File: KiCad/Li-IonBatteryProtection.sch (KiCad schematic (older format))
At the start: 55 parts, among them J1 CONN_02X03, J2 CONN_01X02, Q1 IRF540N, Q2 2N2222A, Q3 2N2222A, Q4 2N2222A, Q5 2N2222A, Q6 2N2222A, U1 LM311N, U2 PC817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

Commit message: Updated the TO-220 footprint. Started fill zones.
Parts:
- Q1: footprint TO_SOT_Packages_THT:TO-220_Neutral123_Horizontal_LargePads -> TO_SOT_Packages_THT:TO-220_Neutral123_Horizontal
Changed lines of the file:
@@
 F 0 "Q1" H 7950 3850 50  0000 L CNN
 F 1 "IRF540N" H 7450 3400 50  0000 L CNN
-F 2 "TO_SOT_Packages_THT:TO-220_Neutral123_Horizontal_LargePads" H 8000 3575 50  0001 L CIN
+F 2 "TO_SOT_Packages_THT:TO-220_Neutral123_Horizontal" H 8000 3575 50  0001 L CIN
 F 3 "" H 7750 3650 50  0000 L CNN
 	1    7750 3650

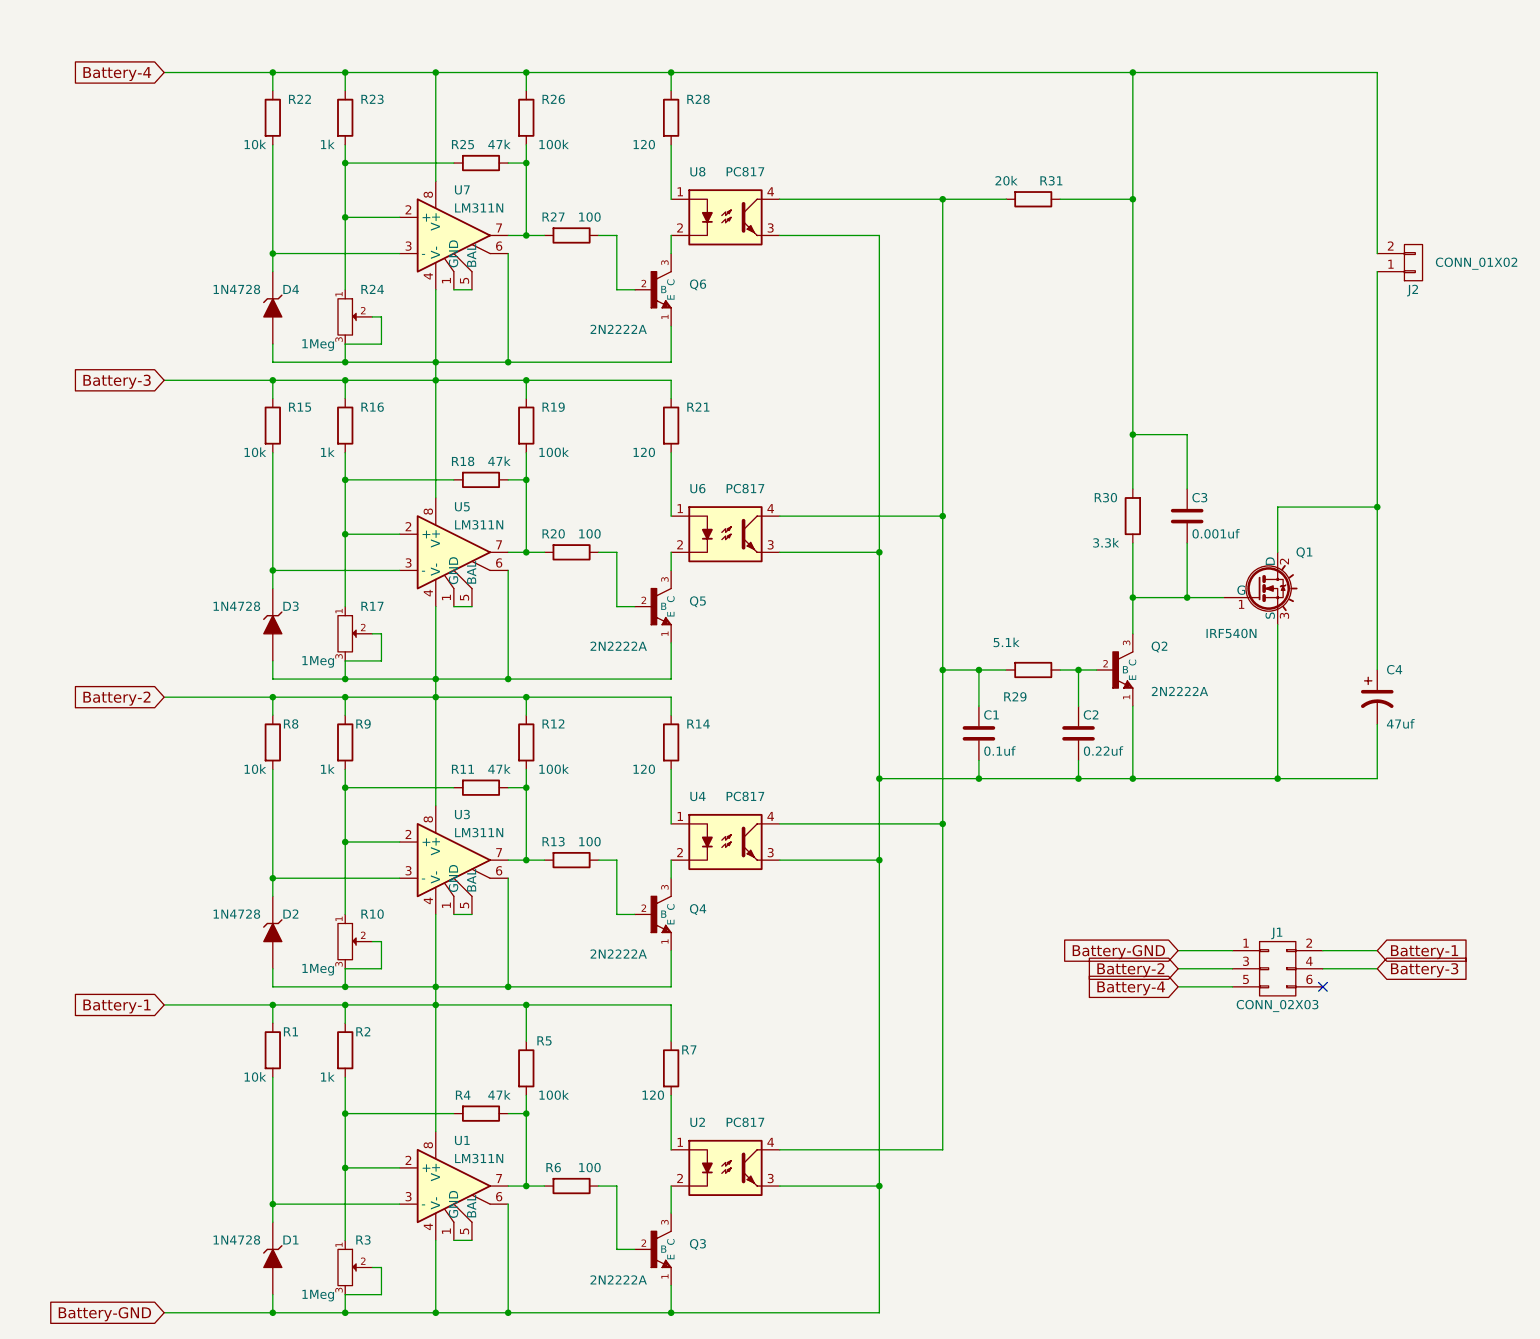
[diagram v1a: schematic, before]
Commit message: Added test points to the schematic.
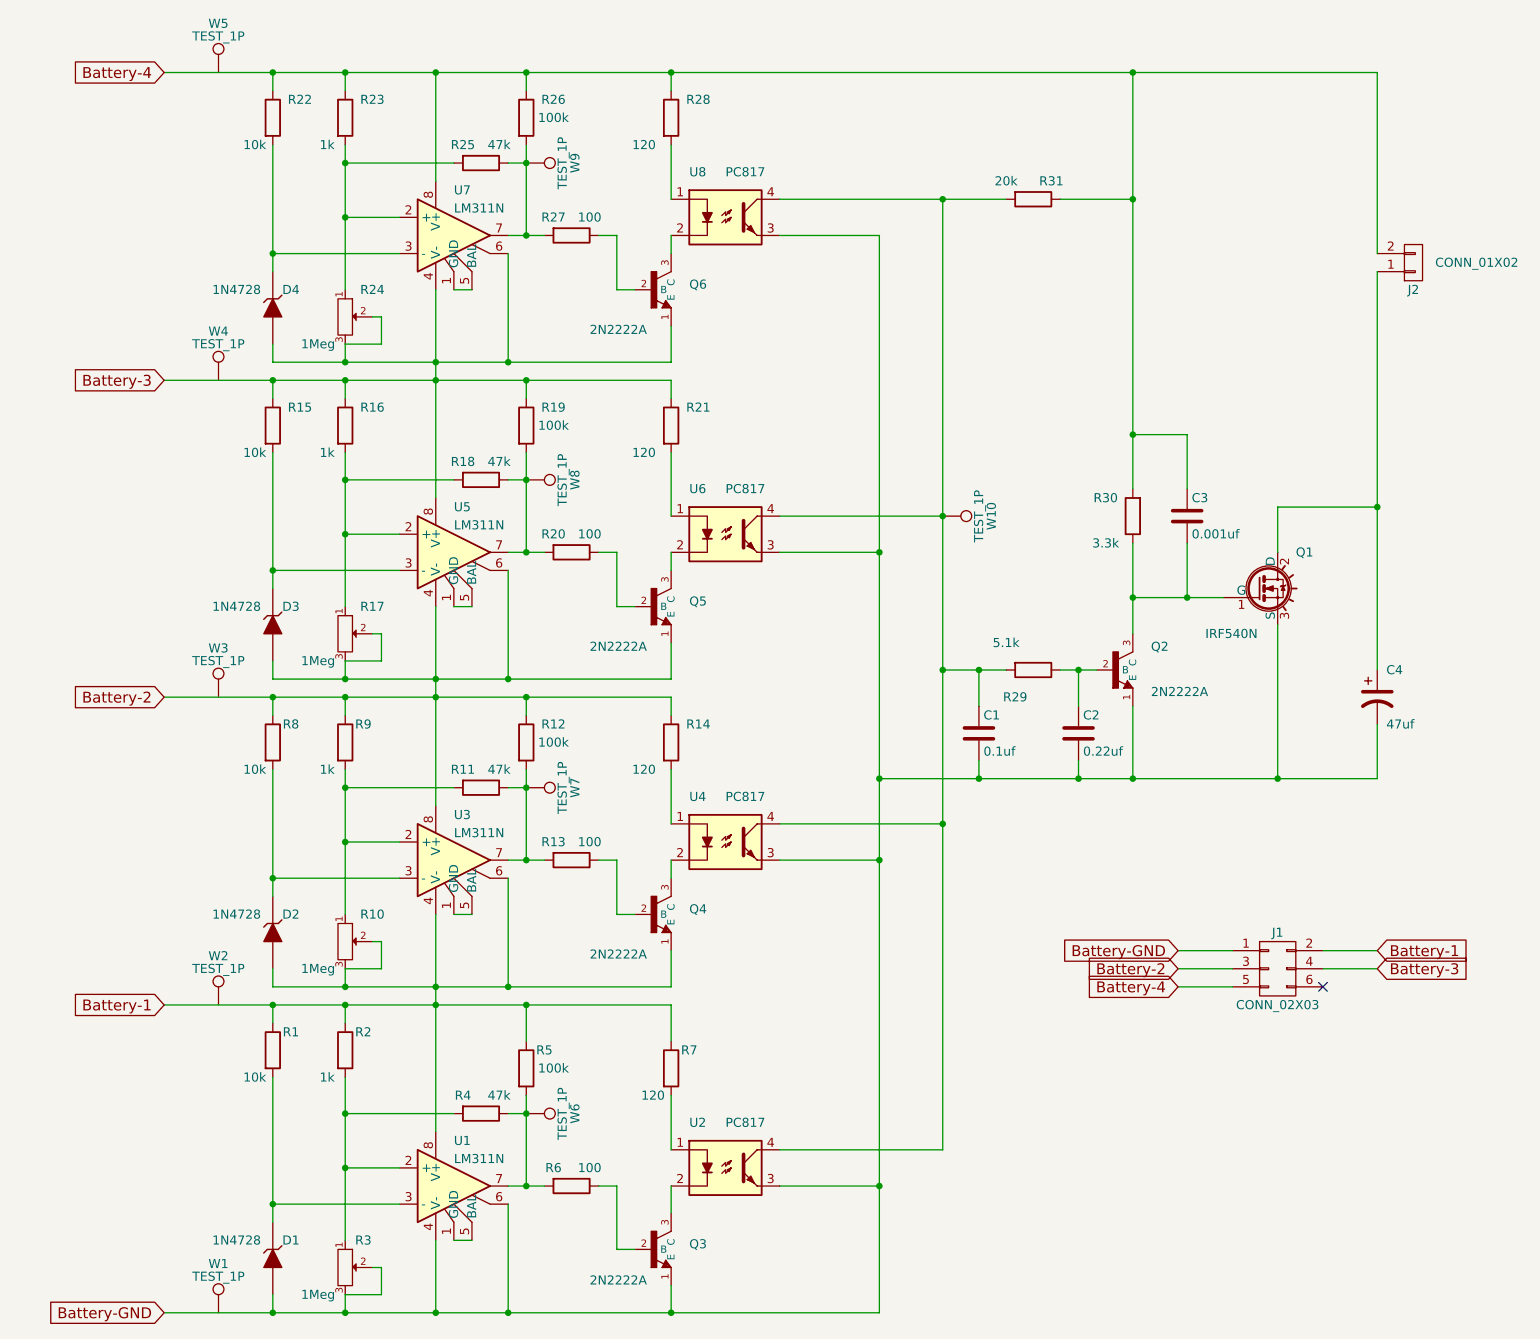
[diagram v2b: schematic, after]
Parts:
- added W1, W10, W2, W3, W4, W5, W6, W7, W8, W9: TEST_1P, Measurement_Points:Measurement_Point_Round-TH_Big, symbol TEST_1P
- R16, R2, R23, R9: footprint Resistors_ThroughHole:Resistor_Horizontal_RM7mm -> Resistors_ThroughHole:Resistor_Horizontal_RM10mm
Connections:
- net at C1.1, R29.2, R31.2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: now also W10.1
- net at R4.1, R5.2, R6.2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: now also W6.1
- net at R11.1, R12.2, R13.2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: now also W7.1
- net at R18.1, R19.2, R20.2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: now also W8.1
- net at R25.1, R26.2, R27.2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: now also W9.1
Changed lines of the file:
@@
 F 0 "R2" H 2800 6300 50  0000 C CNN
 F 1 "1k" H 2600 6050 50  0000 C CNN
-F 2 "Resistors_ThroughHole:Resistor_Horizontal_RM7mm" V 2630 6200 50  0001 C CNN
+F 2 "Resistors_ThroughHole:Resistor_Horizontal_RM10mm" V 2630 6200 50  0001 C CNN
 F 3 "" H 2700 6200 50  0000 C CNN
 	1    2700 6200
@@
 U 1 1 592CD4C8
 P 3700 6300
-F 0 "R5" H 3800 6450 50  0000 C CNN
-F 1 "100k" H 3850 6150 50  0000 C CNN
+F 0 "R5" H 3800 6400 50  0000 C CNN
+F 1 "100k" H 3850 6300 50  0000 C CNN
 F 2 "Resistors_ThroughHole:Resistor_Horizontal_RM10mm" V 3630 6300 50  0001 C CNN
 F 3 "" H 3700 6300 50  0000 C CNN
@@
 F 0 "R9" H 2800 4600 50  0000 C CNN
 F 1 "1k" H 2600 4350 50  0000 C CNN
-F 2 "Resistors_ThroughHole:Resistor_Horizontal_RM7mm" V 2630 4500 50  0001 C CNN
+F 2 "Resistors_ThroughHole:Resistor_Horizontal_RM10mm" V 2630 4500 50  0001 C CNN
 F 3 "" H 2700 4500 50  0000 C CNN
 	1    2700 4500
@@
 P 3700 4500
 F 0 "R12" H 3850 4600 50  0000 C CNN
-F 1 "100k" H 3850 4350 50  0000 C CNN
+F 1 "100k" H 3850 4500 50  0000 C CNN
 F 2 "Resistors_ThroughHole:Resistor_Horizontal_RM10mm" V 3630 4500 50  0001 C CNN
 F 3 "" H 3700 4500 50  0000 C CNN
@@
 F 0 "R16" H 2850 2850 50  0000 C CNN
 F 1 "1k" H 2600 2600 50  0000 C CNN
-F 2 "Resistors_ThroughHole:Resistor_Horizontal_RM7mm" V 2630 2750 50  0001 C CNN
+F 2 "Resistors_ThroughHole:Resistor_Horizontal_RM10mm" V 2630 2750 50  0001 C CNN
 F 3 "" H 2700 2750 50  0000 C CNN
 	1    2700 2750
@@
 P 3700 2750
 F 0 "R19" H 3850 2850 50  0000 C CNN
-F 1 "100k" H 3850 2600 50  0000 C CNN
+F 1 "100k" H 3850 2750 50  0000 C CNN
 F 2 "Resistors_ThroughHole:Resistor_Horizontal_RM10mm" V 3630 2750 50  0001 C CNN
 F 3 "" H 3700 2750 50  0000 C CNN
@@
 F 0 "R23" H 2850 1150 50  0000 C CNN
 F 1 "1k" H 2600 900 50  0000 C CNN
-F 2 "Resistors_ThroughHole:Resistor_Horizontal_RM7mm" V 2630 1050 50  0001 C CNN
+F 2 "Resistors_ThroughHole:Resistor_Horizontal_RM10mm" V 2630 1050 50  0001 C CNN
 F 3 "" H 2700 1050 50  0000 C CNN
 	1    2700 1050
@@
 P 3700 1050
 F 0 "R26" H 3850 1150 50  0000 C CNN
-F 1 "100k" H 3850 900 50  0000 C CNN
+F 1 "100k" H 3850 1050 50  0000 C CNN
 F 2 "Resistors_ThroughHole:Resistor_Horizontal_RM10mm" V 3630 1050 50  0001 C CNN
 F 3 "" H 3700 1050 50  0000 C CNN
@@
 Wire Wire Line
 	2300 1200 2300 1900
+$Comp
+L TEST_1P W1
+U 1 1 5957C591
+P 2000 7650
+F 0 "W1" H 2000 7920 50  0000 C CNN
+F 1 "TEST_1P" H 2000 7850 50  0000 C CNN
+F 2 "Measurement_Points:Measurement_Point_Round-TH_Big" H 2200 7650 50  0001 C CNN
+F 3 "" H 2200 7650 50  0000 C CNN
+	1    2000 7650
+	1    0    0    -1
+$EndComp
+$Comp
+L TEST_1P W2
+U 1 1 5957C682
+P 2000 5950
+F 0 "W2" H 2000 6220 50  0000 C CNN
+F 1 "TEST_1P" H 2000 6150 50  0000 C CNN
+F 2 "Measurement_Points:Measurement_Point_Round-TH_Big" H 2200 5950 50  0001 C CNN
+F 3 "" H 2200 5950 50  0000 C CNN
+	1    2000 5950
+	1    0    0    -1
+$EndComp
+$Comp
+L TEST_1P W3
+U 1 1 5957C733
+P 2000 4250
+F 0 "W3" H 2000 4520 50  0000 C CNN
+F 1 "TEST_1P" H 2000 4450 50  0000 C CNN
+F 2 "Measurement_Points:Measurement_Point_Round-TH_Big" H 2200 4250 50  0001 C CNN
+F 3 "" H 2200 4250 50  0000 C CNN
+	1    2000 4250
+	1    0    0    -1
+$EndComp
+$Comp
+L TEST_1P W4
+U 1 1 5957C7BC
+P 2000 2500
+F 0 "W4" H 2000 2770 50  0000 C CNN
+F 1 "TEST_1P" H 2000 2700 50  0000 C CNN
+F 2 "Measurement_Points:Measurement_Point_Round-TH_Big" H 2200 2500 50  0001 C CNN
+F 3 "" H 2200 2500 50  0000 C CNN
+	1    2000 2500
+	1    0    0    -1
+$EndComp
+$Comp
+L TEST_1P W5
+U 1 1 5957C889
+P 2000 800
+F 0 "W5" H 2000 1070 50  0000 C CNN
+F 1 "TEST_1P" H 2000 1000 50  0000 C CNN
+F 2 "Measurement_Points:Measurement_Point_Round-TH_Big" H 2200 800 50  0001 C CNN
+F 3 "" H 2200 800 50  0000 C CNN
+	1    2000 800
+	1    0    0    -1
+$EndComp
+$Comp
+L TEST_1P W6
+U 1 1 5957D045
+P 3700 6550
+F 0 "W6" H 3700 6820 50  0000 C CNN
+F 1 "TEST_1P" H 3700 6750 50  0000 C CNN
+F 2 "Measurement_Points:Measurement_Point_Round-TH_Big" H 3900 6550 50  0001 C CNN
+F 3 "" H 3900 6550 50  0000 C CNN
+	1    3700 6550
+	0    1    1    0
+$EndComp
+$Comp
+L TEST_1P W7
+U 1 1 5957D1F2
+P 3700 4750
+F 0 "W7" H 3700 5020 50  0000 C CNN
+F 1 "TEST_1P" H 3700 4950 50  0000 C CNN
+F 2 "Measurement_Points:Measurement_Point_Round-TH_Big" H 3900 4750 50  0001 C CNN
+F 3 "" H 3900 4750 50  0000 C CNN
+	1    3700 4750
+	0    1    1    0
+$EndComp
+$Comp
+L TEST_1P W8
+U 1 1 5957D29D
+P 3700 3050
+F 0 "W8" H 3700 3320 50  0000 C CNN
+F 1 "TEST_1P" H 3700 3250 50  0000 C CNN
+F 2 "Measurement_Points:Measurement_Point_Round-TH_Big" H 3900 3050 50  0001 C CNN
+F 3 "" H 3900 3050 50  0000 C CNN
+	1    3700 3050
+	0    1    1    0
+$EndComp
+$Comp
+L TEST_1P W9
+U 1 1 5957D346
+P 3700 1300
+F 0 "W9" H 3700 1570 50  0000 C CNN
+F 1 "TEST_1P" H 3700 1500 50  0000 C CNN
+F 2 "Measurement_Points:Measurement_Point_Round-TH_Big" H 3900 1300 50  0001 C CNN
+F 3 "" H 3900 1300 50  0000 C CNN
+	1    3700 1300
+	0    1    1    0
+$EndComp
+$Comp
+L TEST_1P W10
+U 1 1 5957E037
+P 6000 3250
+F 0 "W10" H 6000 3520 50  0000 C CNN
+F 1 "TEST_1P" H 6000 3450 50  0000 C CNN
+F 2 "Measurement_Points:Measurement_Point_Round-TH_Big" H 6200 3250 50  0001 C CNN
+F 3 "" H 6200 3250 50  0000 C CNN
+	1    6000 3250
+	0    1    1    0
+$EndComp
 $EndSCHEMATC

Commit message: Updated the source files.
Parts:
- added TP11: TEST_1P, Measurement_Points:Measurement_Point_Round-TH_Small, symbol TEST_1P
- TP1: renamed from W1; footprint Measurement_Points:Measurement_Point_Round-TH_Big -> Measurement_Points:Measurement_Point_Round-TH_Small
- TP10: renamed from W10; footprint Measurement_Points:Measurement_Point_Round-TH_Big -> Measurement_Points:Measurement_Point_Round-TH_Small
- TP2: renamed from W2; footprint Measurement_Points:Measurement_Point_Round-TH_Big -> Measurement_Points:Measurement_Point_Round-TH_Small
- TP3: renamed from W3; footprint Measurement_Points:Measurement_Point_Round-TH_Big -> Measurement_Points:Measurement_Point_Round-TH_Small
- TP4: renamed from W4; footprint Measurement_Points:Measurement_Point_Round-TH_Big -> Measurement_Points:Measurement_Point_Round-TH_Small
- TP5: renamed from W5; footprint Measurement_Points:Measurement_Point_Round-TH_Big -> Measurement_Points:Measurement_Point_Round-TH_Small
- TP6: renamed from W6; footprint Measurement_Points:Measurement_Point_Round-TH_Big -> Measurement_Points:Measurement_Point_Round-TH_Small
- TP7: renamed from W7; footprint Measurement_Points:Measurement_Point_Round-TH_Big -> Measurement_Points:Measurement_Point_Round-TH_Small
- TP8: renamed from W8; footprint Measurement_Points:Measurement_Point_Round-TH_Big -> Measurement_Points:Measurement_Point_Round-TH_Small
- TP9: renamed from W9; footprint Measurement_Points:Measurement_Point_Round-TH_Big -> Measurement_Points:Measurement_Point_Round-TH_Small
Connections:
- net Battery-1: now also TP2.1
- net Battery-2: now also TP3.1
- net Battery-3: now also TP4.1
- net Battery-4: now also TP5.1
- net Battery-GND: now also TP1.1
- net at C3.2, Q1.1 (G), Q2.3 (C)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: now also TP11.1
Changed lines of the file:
@@
 	2300 1200 2300 1900
 $Comp
-L TEST_1P W1
+L TEST_1P TP1
 U 1 1 5957C591
 P 2000 7650
-F 0 "W1" H 2000 7920 50  0000 C CNN
-F 1 "TEST_1P" H 2000 7850 50  0000 C CNN
-F 2 "Measurement_Points:Measurement_Point_Round-TH_Big" H 2200 7650 50  0001 C CNN
+F 0 "TP1" H 2000 7850 50  0000 C CNN
+F 1 "TEST_1P" H 2000 7850 50  0001 C CNN
+F 2 "Measurement_Points:Measurement_Point_Round-TH_Small" H 2200 7650 50  0001 C CNN
 F 3 "" H 2200 7650 50  0000 C CNN
 	1    2000 7650
@@
 $EndComp
 $Comp
-L TEST_1P W2
+L TEST_1P TP2
 U 1 1 5957C682
 P 2000 5950
-F 0 "W2" H 2000 6220 50  0000 C CNN
-F 1 "TEST_1P" H 2000 6150 50  0000 C CNN
-F 2 "Measurement_Points:Measurement_Point_Round-TH_Big" H 2200 5950 50  0001 C CNN
+F 0 "TP2" H 2000 6150 50  0000 C CNN
+F 1 "TEST_1P" H 2000 6150 50  0001 C CNN
+F 2 "Measurement_Points:Measurement_Point_Round-TH_Small" H 2200 5950 50  0001 C CNN
 F 3 "" H 2200 5950 50  0000 C CNN
 	1    2000 5950
@@
 $EndComp
 $Comp
-L TEST_1P W3
+L TEST_1P TP3
 U 1 1 5957C733
 P 2000 4250
-F 0 "W3" H 2000 4520 50  0000 C CNN
-F 1 "TEST_1P" H 2000 4450 50  0000 C CNN
-F 2 "Measurement_Points:Measurement_Point_Round-TH_Big" H 2200 4250 50  0001 C CNN
+F 0 "TP3" H 2000 4450 50  0000 C CNN
+F 1 "TEST_1P" H 2000 4450 50  0001 C CNN
+F 2 "Measurement_Points:Measurement_Point_Round-TH_Small" H 2200 4250 50  0001 C CNN
 F 3 "" H 2200 4250 50  0000 C CNN
 	1    2000 4250
@@
 $EndComp
 $Comp
-L TEST_1P W4
+L TEST_1P TP4
 U 1 1 5957C7BC
 P 2000 2500
-F 0 "W4" H 2000 2770 50  0000 C CNN
-F 1 "TEST_1P" H 2000 2700 50  0000 C CNN
-F 2 "Measurement_Points:Measurement_Point_Round-TH_Big" H 2200 2500 50  0001 C CNN
+F 0 "TP4" H 2000 2700 50  0000 C CNN
+F 1 "TEST_1P" H 2000 2700 50  0001 C CNN
+F 2 "Measurement_Points:Measurement_Point_Round-TH_Small" H 2200 2500 50  0001 C CNN
 F 3 "" H 2200 2500 50  0000 C CNN
 	1    2000 2500
@@
 $EndComp
 $Comp
-L TEST_1P W5
+L TEST_1P TP5
 U 1 1 5957C889
 P 2000 800
-F 0 "W5" H 2000 1070 50  0000 C CNN
-F 1 "TEST_1P" H 2000 1000 50  0000 C CNN
-F 2 "Measurement_Points:Measurement_Point_Round-TH_Big" H 2200 800 50  0001 C CNN
+F 0 "TP5" H 2000 1000 50  0000 C CNN
+F 1 "TEST_1P" H 2000 1000 50  0001 C CNN
+F 2 "Measurement_Points:Measurement_Point_Round-TH_Small" H 2200 800 50  0001 C CNN
 F 3 "" H 2200 800 50  0000 C CNN
 	1    2000 800
@@
 $EndComp
 $Comp
-L TEST_1P W6
+L TEST_1P TP6
 U 1 1 5957D045
 P 3700 6550
-F 0 "W6" H 3700 6820 50  0000 C CNN
-F 1 "TEST_1P" H 3700 6750 50  0000 C CNN
-F 2 "Measurement_Points:Measurement_Point_Round-TH_Big" H 3900 6550 50  0001 C CNN
+F 0 "TP6" V 3700 6820 50  0000 C CNN
+F 1 "TEST_1P" H 3700 6750 50  0001 C CNN
+F 2 "Measurement_Points:Measurement_Point_Round-TH_Small" H 3900 6550 50  0001 C CNN
 F 3 "" H 3900 6550 50  0000 C CNN
 	1    3700 6550
@@
 $EndComp
 $Comp
-L TEST_1P W7
+L TEST_1P TP7
 U 1 1 5957D1F2
 P 3700 4750
-F 0 "W7" H 3700 5020 50  0000 C CNN
-F 1 "TEST_1P" H 3700 4950 50  0000 C CNN
-F 2 "Measurement_Points:Measurement_Point_Round-TH_Big" H 3900 4750 50  0001 C CNN
+F 0 "TP7" V 3700 5020 50  0000 C CNN
+F 1 "TEST_1P" H 3700 4950 50  0001 C CNN
+F 2 "Measurement_Points:Measurement_Point_Round-TH_Small" H 3900 4750 50  0001 C CNN
 F 3 "" H 3900 4750 50  0000 C CNN
 	1    3700 4750
@@
 $EndComp
 $Comp
-L TEST_1P W8
+L TEST_1P TP8
 U 1 1 5957D29D
 P 3700 3050
-F 0 "W8" H 3700 3320 50  0000 C CNN
-F 1 "TEST_1P" H 3700 3250 50  0000 C CNN
-F 2 "Measurement_Points:Measurement_Point_Round-TH_Big" H 3900 3050 50  0001 C CNN
+F 0 "TP8" V 3700 3320 50  0000 C CNN
+F 1 "TEST_1P" H 3700 3250 50  0001 C CNN
+F 2 "Measurement_Points:Measurement_Point_Round-TH_Small" H 3900 3050 50  0001 C CNN
 F 3 "" H 3900 3050 50  0000 C CNN
 	1    3700 3050
@@
 $EndComp
 $Comp
-L TEST_1P W9
+L TEST_1P TP9
 U 1 1 5957D346
 P 3700 1300
-F 0 "W9" H 3700 1570 50  0000 C CNN
-F 1 "TEST_1P" H 3700 1500 50  0000 C CNN
-F 2 "Measurement_Points:Measurement_Point_Round-TH_Big" H 3900 1300 50  0001 C CNN
+F 0 "TP9" V 3700 1570 50  0000 C CNN
+F 1 "TEST_1P" H 3700 1500 50  0001 C CNN
+F 2 "Measurement_Points:Measurement_Point_Round-TH_Small" H 3900 1300 50  0001 C CNN
 F 3 "" H 3900 1300 50  0000 C CNN
 	1    3700 1300
@@
 $EndComp
 $Comp
-L TEST_1P W10
+L TEST_1P TP10
 U 1 1 5957E037
 P 6000 3250
-F 0 "W10" H 6000 3520 50  0000 C CNN
-F 1 "TEST_1P" H 6000 3450 50  0000 C CNN
-F 2 "Measurement_Points:Measurement_Point_Round-TH_Big" H 6200 3250 50  0001 C CNN
+F 0 "TP10" V 6000 3520 50  0000 C CNN
+F 1 "TEST_1P" H 6000 3450 50  0001 C CNN
+F 2 "Measurement_Points:Measurement_Point_Round-TH_Small" H 6200 3250 50  0001 C CNN
 F 3 "" H 6200 3250 50  0000 C CNN
 	1    6000 3250
 	0    1    1    0
 $EndComp
+Connection ~ 2000 7650
+Connection ~ 2000 5950
+Connection ~ 2000 4250
+Connection ~ 2000 2500
+Connection ~ 2000 800
+$Comp
+L TEST_1P TP11
+U 1 1 595800FC
+P 7050 3700
+F 0 "TP11" V 7050 3970 50  0000 C CNN
+F 1 "TEST_1P" H 7050 3900 50  0001 C CNN
+F 2 "Measurement_Points:Measurement_Point_Round-TH_Small" H 7250 3700 50  0001 C CNN
+F 3 "" H 7250 3700 50  0000 C CNN
+	1    7050 3700
+	0    -1   -1   0
+$EndComp
 $EndSCHEMATC
